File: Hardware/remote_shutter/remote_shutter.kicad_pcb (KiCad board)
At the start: 4 copper layers, 78 x 57 mm, 66 parts, among them J1 USB_C_Receptacle_USB2.0, J2 OLED, J3 AudioJack3, J4 Buzzer, J5 Conn_01x02_Male, J6 Switch, J7 Conn_01x06_Male, Q1 DMN2056U, Q2 DMN2056U, Q3 BC847BDW1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

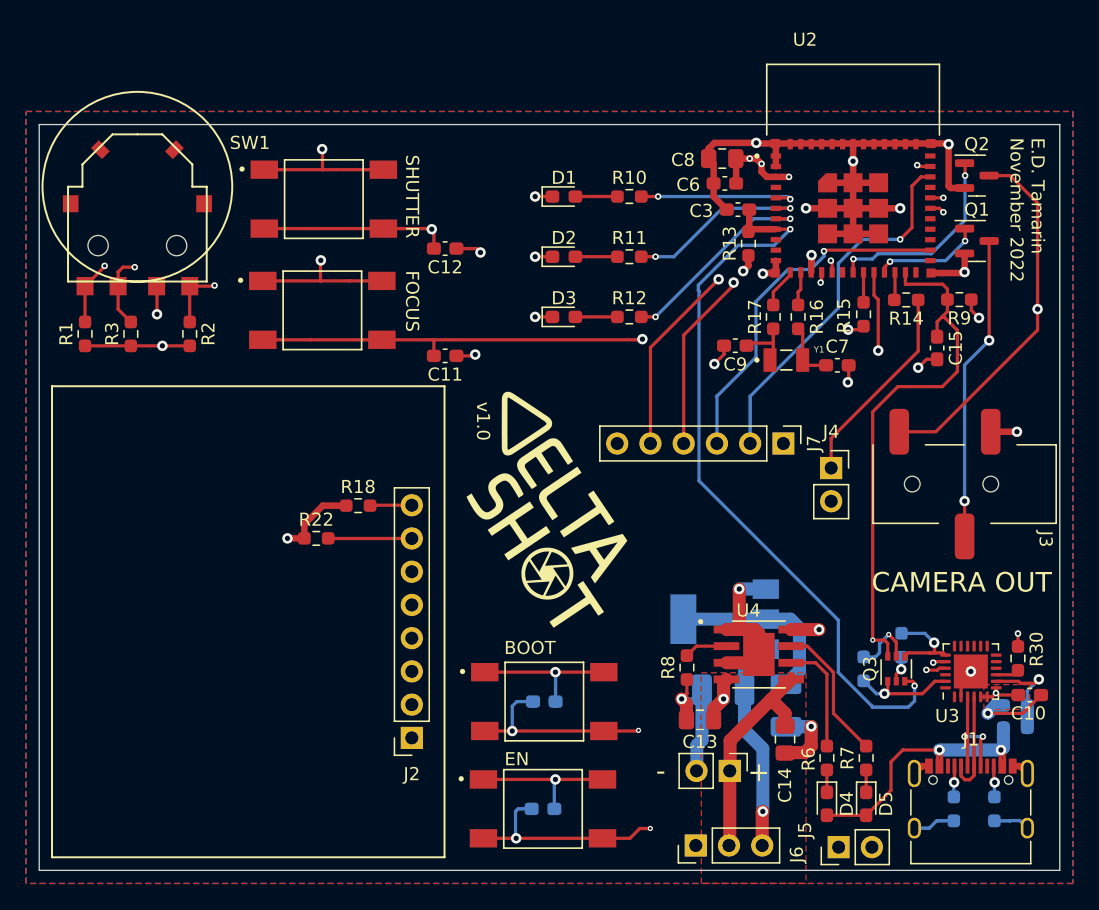
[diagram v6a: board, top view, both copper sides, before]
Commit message: Changing layout & updated ESP footprint
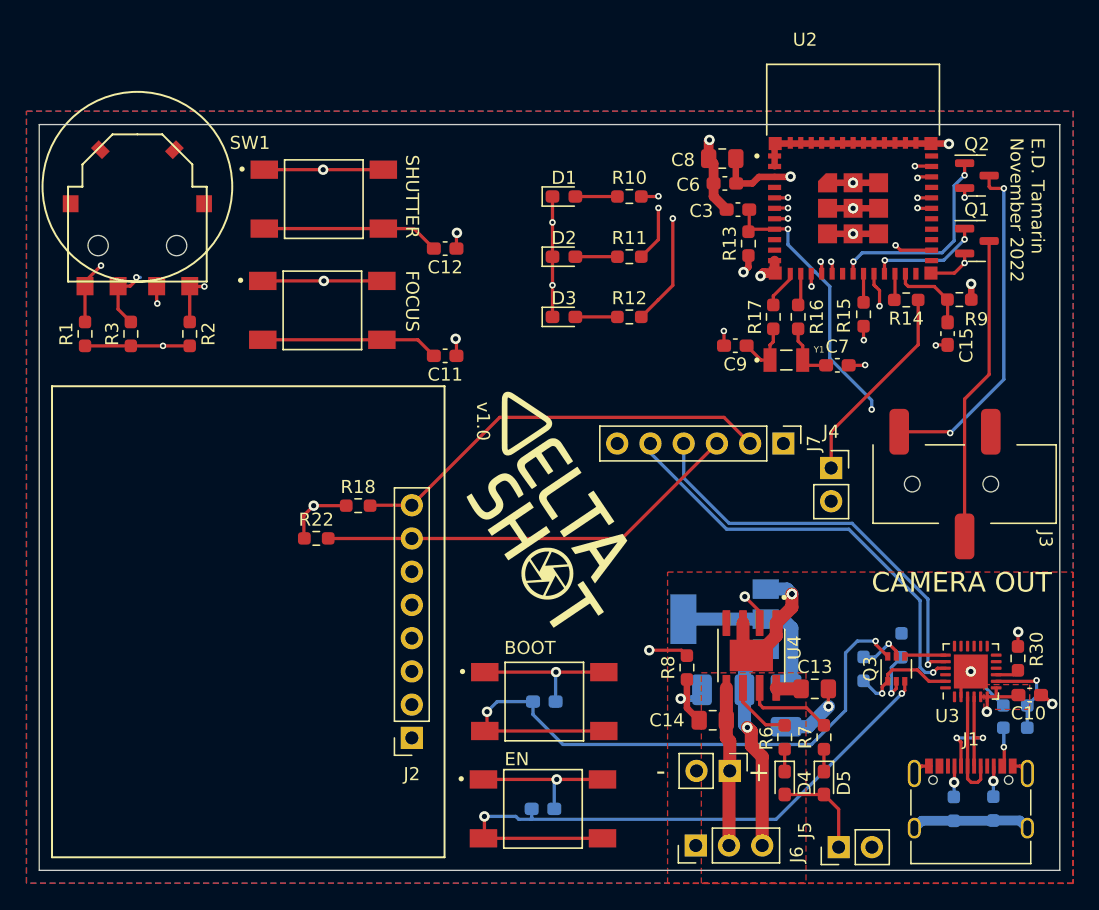
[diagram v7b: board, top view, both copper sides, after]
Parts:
- moved C13 9.09 mm to (163.8, 112.2), turned to 0 degrees
- moved C14 5.72 mm to (155.9, 114.5), turned to 180 degrees
- moved D4 3.60 mm to (161.4, 119.3)
- moved D5 3.60 mm to (164.4, 119.3)
- moved R6 3.60 mm to (161.4, 115.8)
- moved R7 3.60 mm to (164.4, 115.8)
- moved C15 1.36 mm to (173.9, 85.0)
- moved U4 0.58 mm to (158.9, 109.6), turned to -90 degrees
- moved R4 0.08 mm to (177.4, 121.3)
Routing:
- net /MCU/Interfaces/SHUTTER: track 97.6 -> 40.0 mm
- net /MCU/Interfaces/FOCUS: track 80.2 -> 36.9 mm, vias 3 -> 0
- net /VBUS: track 52.2 -> 12.4 mm, vias 4 -> 1
- net /MCU/IO0: track 83.9 -> 56.2 mm, vias 3 -> 2
- net GND: track 167.0 -> 139.8 mm
- net /MCU/EN: track 111.4 -> 92.6 mm
- net Net-(R8-Pad2): track 3.32 -> 14.5 mm, vias 0 -> 2
- net /MCU/RST: track 59.0 -> 51.1 mm
- net /MCU/Interfaces/I2C.SCL: track 61.8 -> 56.4 mm
- net /Power/VBAT: track 17.1 -> 12.2 mm
- net Net-(R7-Pad2): track 10.7 -> 6.84 mm
- net /Comms/RTS: track 7.03 -> 3.15 mm, vias 1 -> 0
- net Net-(R6-Pad2): track 8.58 -> 5.01 mm
- net /MCU/TX: track 66.4 -> 69.4 mm, vias 3 -> 2
- net /MCU/RX: track 67.7 -> 70.6 mm, vias 3 -> 2
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- added copper zone on F.Cu, net /VBUS
- added copper zone on In1.Cu, net GND
- removed copper zone on In1.Cu, net (none)
- removed copper zone on In1.Cu, net /VBUS

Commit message: Changed layout for better routing. New routing.
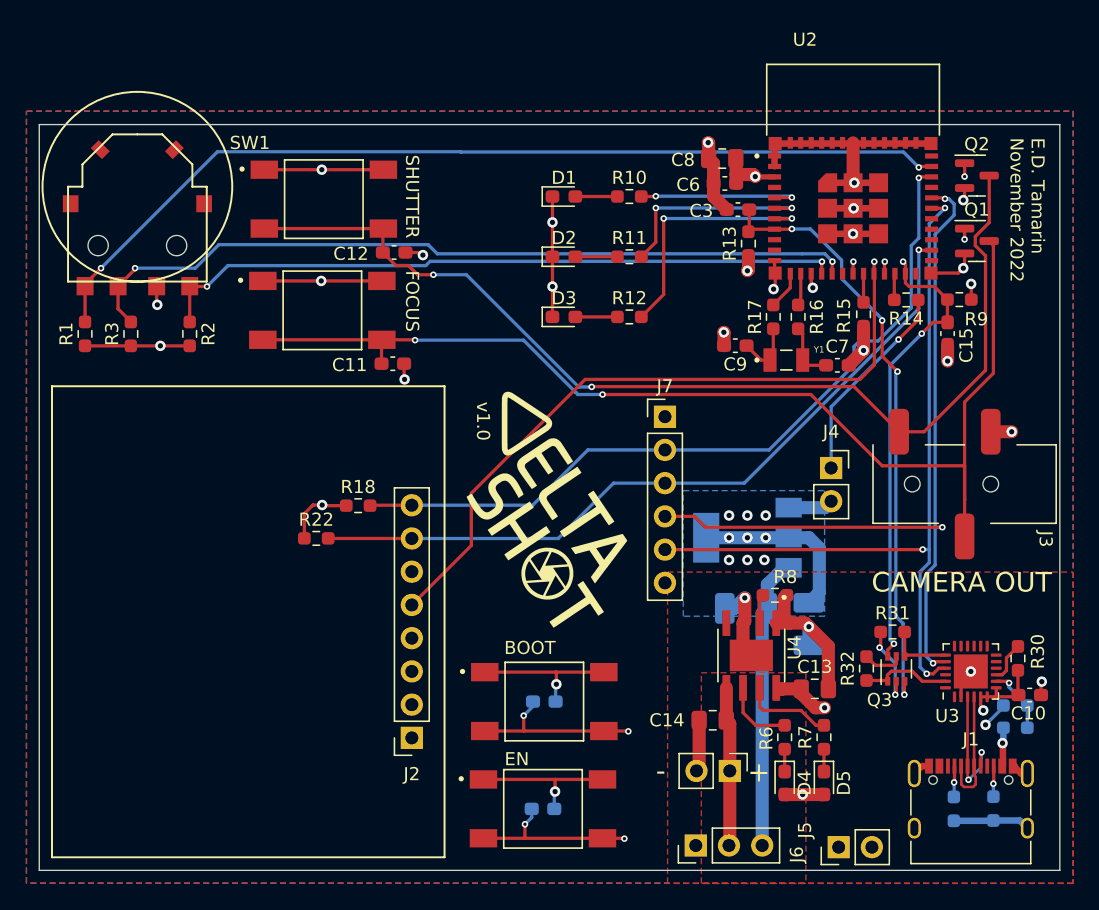
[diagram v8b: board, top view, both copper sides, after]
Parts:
- R31, R32: moved to F.Cu
- moved J7 9.28 mm to (152.3, 91.3), turned to 0 degrees
- moved R8 8.70 mm to (160.7, 105.0), turned to 180 degrees
- moved U1 6.46 mm to (158.6, 100.6)
- moved C1 6.46 mm to (158.5, 106.0)
- moved C2 6.46 mm to (163.3, 107.2)
- moved C11 4.04 mm to (131.5, 87.3)
- moved C12 3.91 mm to (131.6, 78.8)
- moved R31 1.23 mm to (169.7, 107.8), turned to 0 degrees
- moved R32 0.22 mm to (167.7, 110.6)
- turned R30 to 90 degrees
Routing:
- net /MCU/Interfaces/FOCUS: track 36.9 -> 85.7 mm, vias 0 -> 2
- net /MCU/Interfaces/SHUTTER: track 40.0 -> 80.3 mm
- net /MCU/IO0: track 56.2 -> 72.4 mm, vias 2 -> 5
- net Net-(R8-Pad2): track 14.5 -> 2.23 mm, vias 2 -> 0
- net /MCU/RX: track 70.6 -> 59.4 mm, vias 2 -> 3
- net /MCU/TX: track 69.4 -> 61.2 mm, vias 2 -> 3
- net Net-(C1-Pad1): track 16.2 -> 22.3 mm, vias 1 -> 0
- net /MCU/EN: track 92.6 -> 87.2 mm, vias 4 -> 6
- net GND: track 139.8 -> 143.5 mm, vias 28 -> 26
- net /MCU/STRIG: track 15.6 -> 13.2 mm
- net /VBUS: track 12.4 -> 10.1 mm, vias 1 -> 3
- net /MCU/RST: track 51.1 -> 53.2 mm
- net Net-(Q3-Pad2): track 4.17 -> 6.19 mm, vias 1 -> 2
- net Net-(R28-Pad2): track 7.03 -> 5.04 mm
- net /Comms/RTS: track 3.15 -> 4.83 mm
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- added copper zone on B.Cu, net (none)
- added copper zone on In2.Cu, net +3V3
- removed copper zone on F.Cu, net +3V3
- removed copper zone on In2.Cu, net GND
